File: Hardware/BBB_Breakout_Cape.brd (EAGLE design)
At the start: 86.4 x 54.6 mm, 20 parts, among them U1 EEPROM-I2CSMD

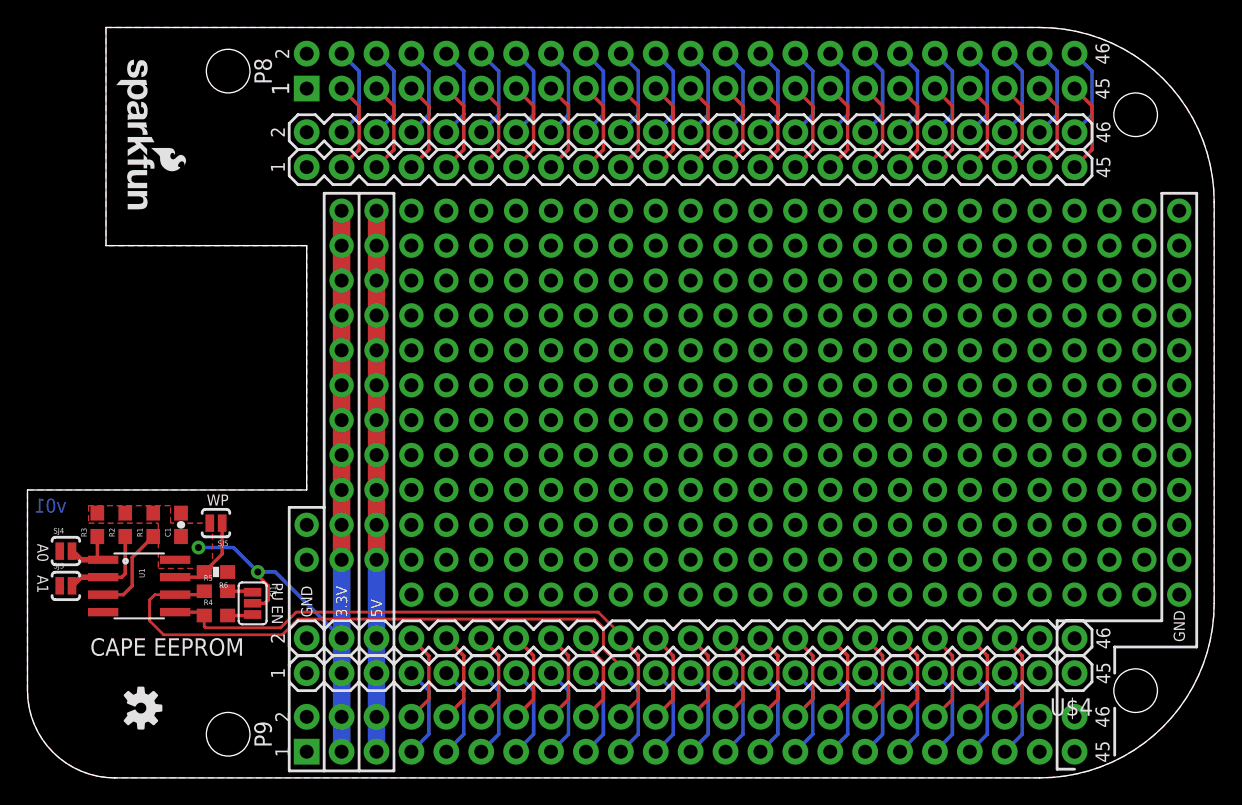
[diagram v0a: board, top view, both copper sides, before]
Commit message: added LEDS
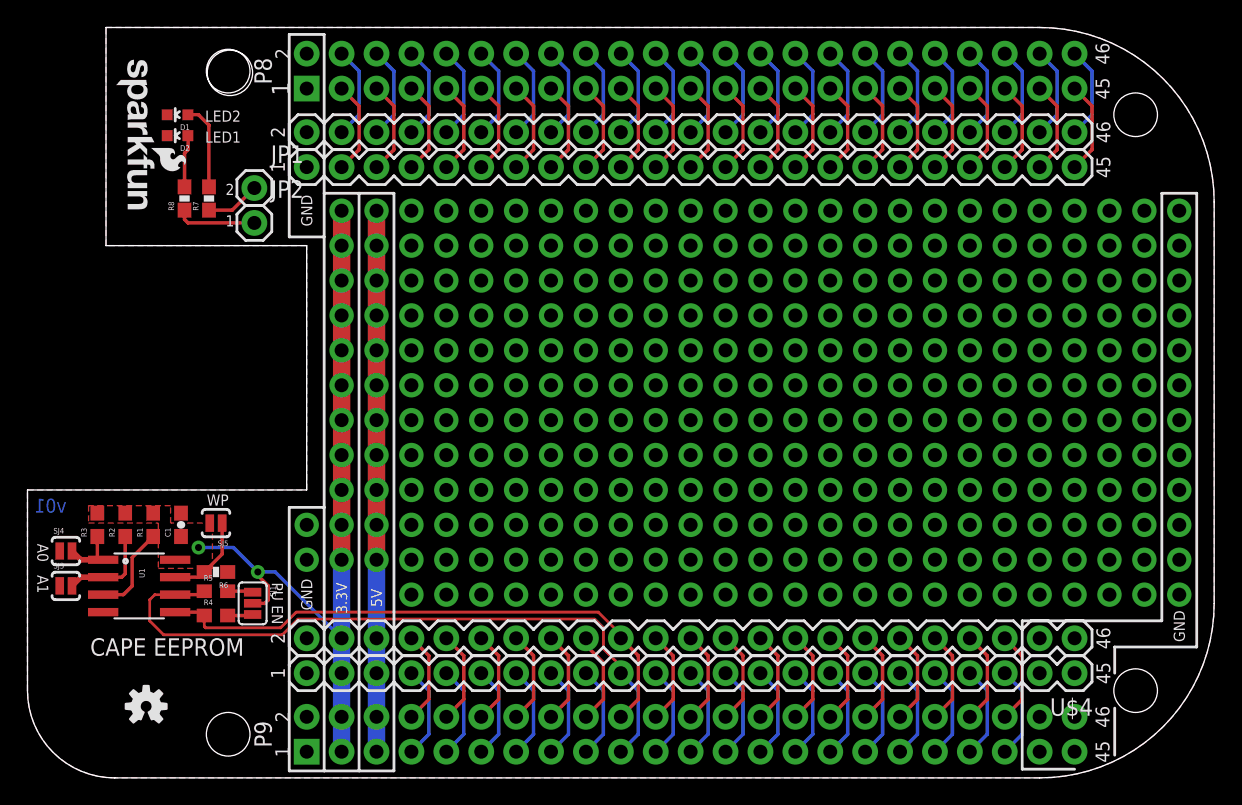
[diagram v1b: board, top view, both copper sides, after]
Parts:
- added D1, D2: RED, SparkFun-LED:LED-0603
- added JP1, JP2: M01PTH, SparkFun-Connectors:1X01
- added R7, R8: 1K, SparkFun-Resistors:0603-RES
- added STANDOFF1: STAND-OFF, SparkFun-Electromechanical:STAND-OFF
- moved LOGO2 0.40 mm to (8.64, 5.21), turned to 0 degrees
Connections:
- new net N$3: D1.A, R7.2
- new net N$30: JP2.1, R8.1
- new net N$7: D2.A, R8.2
- new net N$8: JP1.1, R7.1
- net GND: now also D1.C, D2.C
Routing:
- net N$3: track 0.00 -> 6.34 mm
- net N$30: track 0.00 -> 5.86 mm
- net N$8: track 0.00 -> 3.97 mm
- net N$7: track 0.00 -> 3.83 mm
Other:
- board text added: "LED1"
- board text added: "LED2"

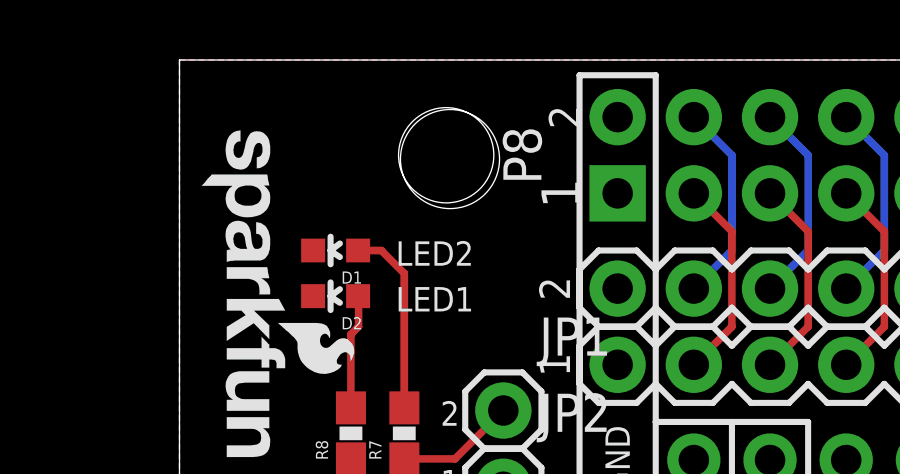
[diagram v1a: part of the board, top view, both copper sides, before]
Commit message: added more labels and fixed drill hole
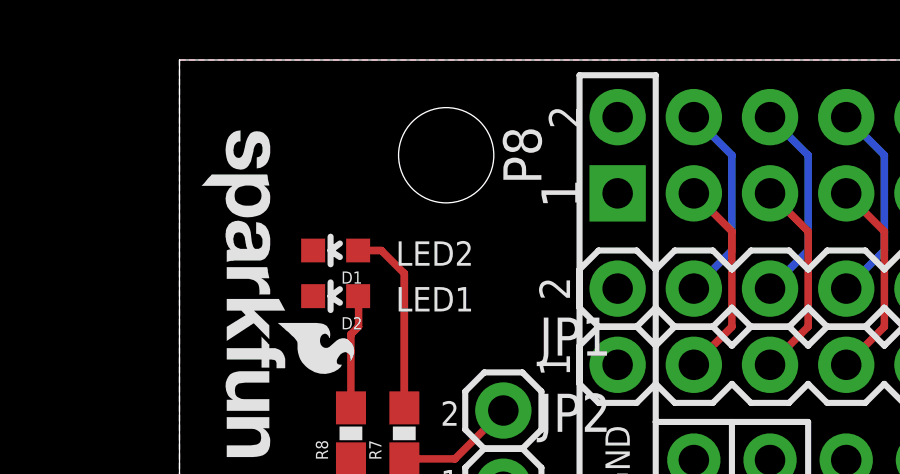
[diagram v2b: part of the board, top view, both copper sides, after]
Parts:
- removed STANDOFF1: STAND-OFF, SparkFun-Electromechanical:STAND-OFF
- added U$6: (no value), SparkFun-Aesthetics:SFE_LOGO_NAME_FLAME_.1
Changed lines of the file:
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@@
 <text x="14.732" y="40.132" size="0.8128" layer="21" font="vector" ratio="15" align="bottom-center">1</text>
 <text x="14.732" y="42.418" size="0.8128" layer="21" font="vector" ratio="15" align="bottom-center">2</text>
+<text x="14.732" y="42.418" size="0.8128" layer="22" font="vector" ratio="15" rot="MR0" align="bottom-center">2</text>
+<text x="14.732" y="40.132" size="0.8128" layer="22" font="vector" ratio="15" rot="MR0" align="bottom-center">1</text>
 </plain>
 <attributes>
@@
 <element name="JP1" library="SparkFun-Connectors" package="1X01" value="M01PTH" x="16.51" y="42.926"/>
 <element name="JP2" library="SparkFun-Connectors" package="1X01" value="M01PTH" x="16.51" y="40.386"/>
-<element name="STANDOFF1" library="SparkFun-Electromechanical" package="STAND-OFF" value="STAND-OFF" x="14.732" y="51.308"/>
+<element name="U$6" library="SparkFun-Aesthetics" package="SFE_LOGO_NAME_FLAME_.1" value="" x="7.874" y="4.318" rot="MR90"/>
 </elements>
 <signals>

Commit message: added version number
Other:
- board text added: "v10"
- board text removed: "v01"
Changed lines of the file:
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@@
 <wire x1="21.59" y1="6.858" x2="21.59" y2="0.508" width="0.2032" layer="21"/>
 <wire x1="24.13" y1="0.508" x2="24.13" y2="6.858" width="0.2032" layer="21"/>
-<text x="0.508" y="20.32" size="1.016" layer="16" font="vector" ratio="15" rot="MR180">v01</text>
+<text x="0.508" y="20.32" size="1.016" layer="16" font="vector" ratio="15" rot="MR180">v10</text>
 <text x="20.32" y="40.132" size="0.8128" layer="22" font="vector" ratio="15" rot="SMR270" align="center-right">GND</text>
 <text x="20.32" y="40.132" size="0.8128" layer="21" font="vector" ratio="15" rot="R270" align="center-right">GND</text>

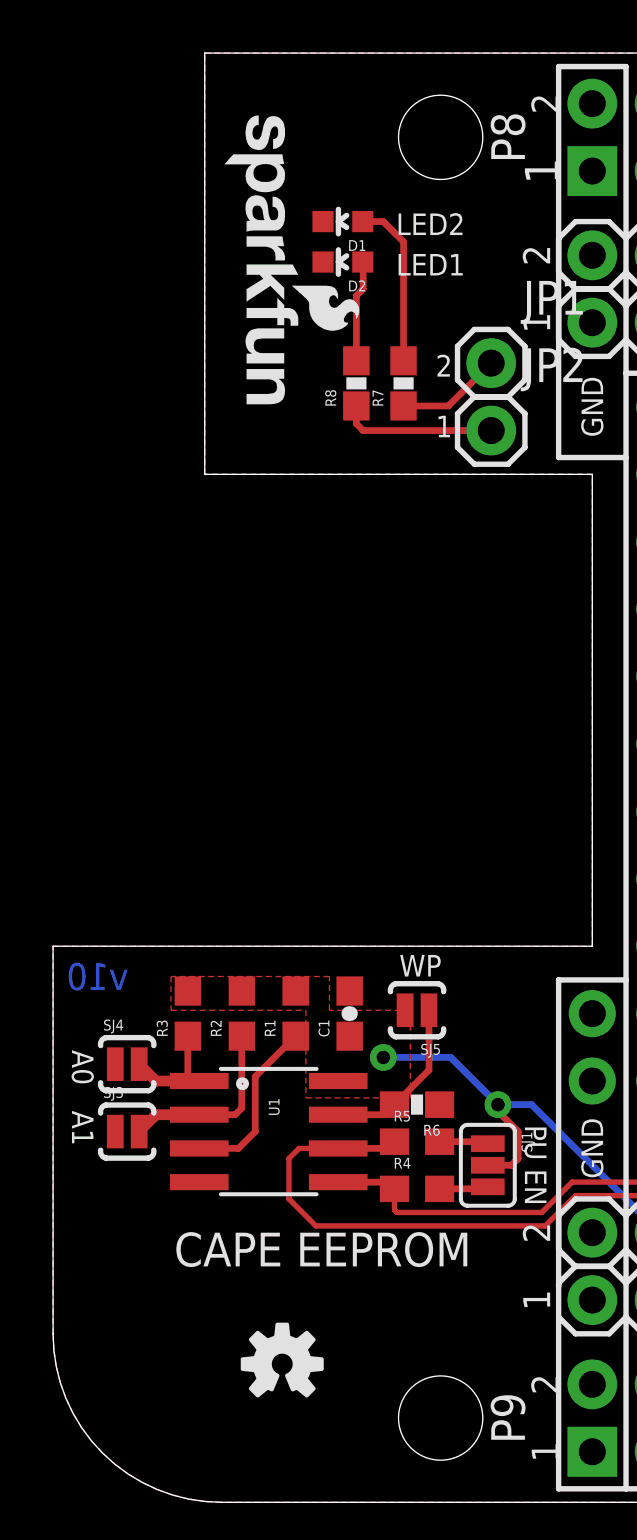
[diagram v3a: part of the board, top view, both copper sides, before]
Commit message: added local fiducials
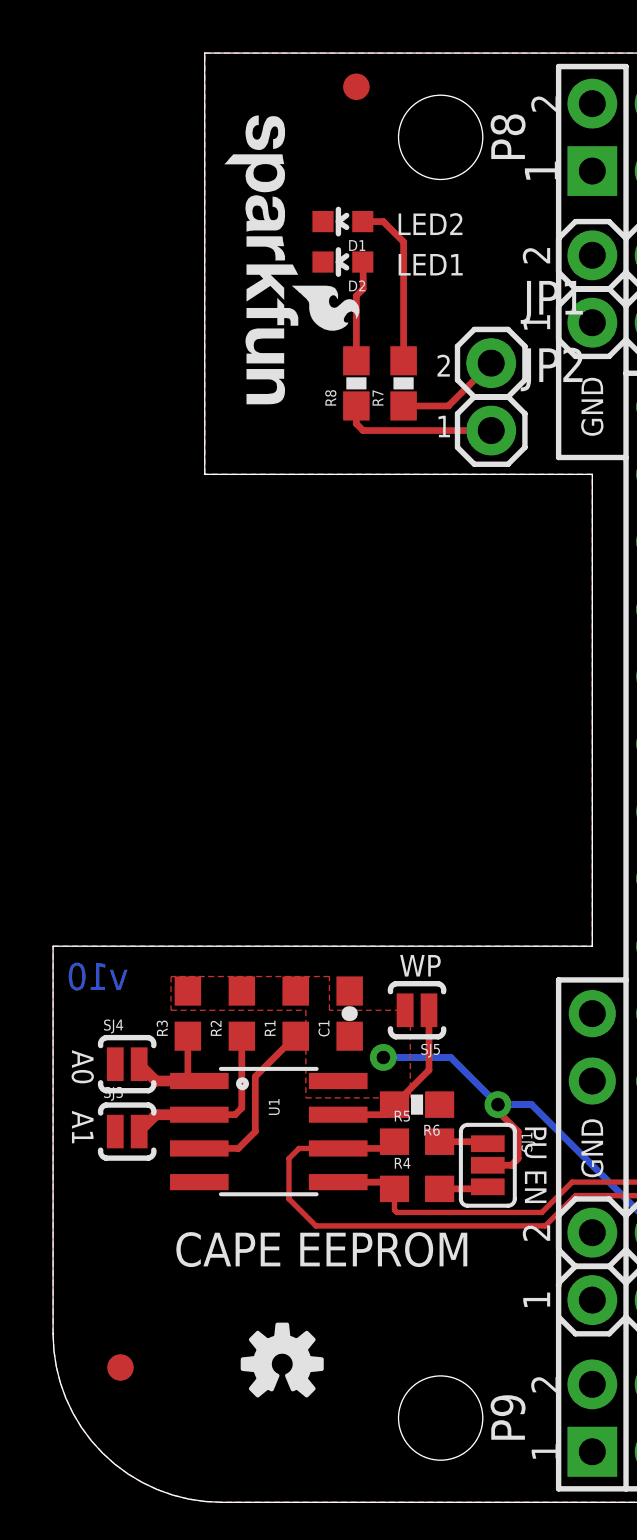
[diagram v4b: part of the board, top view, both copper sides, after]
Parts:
- added FID1, FID2: FIDUCIAL1X2, SparkFun-Aesthetics:FIDUCIAL-1X2
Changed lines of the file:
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@@
 <setting verticaltext="up"/>
 </settings>
-<grid distance="0.01" unitdist="inch" unit="inch" style="lines" multiple="1" display="yes" altdistance="0.005" altunitdist="inch" altunit="inch"/>
+<grid distance="0.05" unitdist="inch" unit="inch" style="lines" multiple="1" display="yes" altdistance="0.01" altunitdist="inch" altunit="inch"/>
 <layers>
 <layer number="1" name="Top" color="4" fill="1" visible="yes" active="yes"/>
@@
 <layer number="18" name="Vias" color="2" fill="1" visible="yes" active="yes"/>
 <layer number="19" name="Unrouted" color="6" fill="1" visible="yes" active="yes"/>
-<layer number="20" name="Dimension" color="15" fill="1" visible="yes" active="yes"/>
-<layer number="21" name="tPlace" color="16" fill="1" visible="yes" active="yes"/>
-<layer number="22" name="bPlace" color="14" fill="1" visible="yes" active="yes"/>
+<layer number="20" name="Dimension" color="6" fill="1" visible="yes" active="yes"/>
+<layer number="21" name="tPlace" color="6" fill="1" visible="yes" active="yes"/>
+<layer number="22" name="bPlace" color="6" fill="1" visible="yes" active="yes"/>
 <layer number="23" name="tOrigins" color="15" fill="1" visible="yes" active="yes"/>
 <layer number="24" name="bOrigins" color="15" fill="1" visible="yes" active="yes"/>
@@
 <element name="JP2" library="SparkFun-Connectors" package="1X01" value="M01PTH" x="16.51" y="40.386"/>
 <element name="U$6" library="SparkFun-Aesthetics" package="SFE_LOGO_NAME_FLAME_.1" value="" x="7.874" y="4.318" rot="MR90"/>
+<element name="FID1" library="SparkFun-Aesthetics" package="FIDUCIAL-1X2" value="FIDUCIAL1X2" x="2.54" y="5.08"/>
+<element name="FID2" library="SparkFun-Aesthetics" package="FIDUCIAL-1X2" value="FIDUCIAL1X2" x="11.43" y="53.34"/>
 </elements>
 <signals>

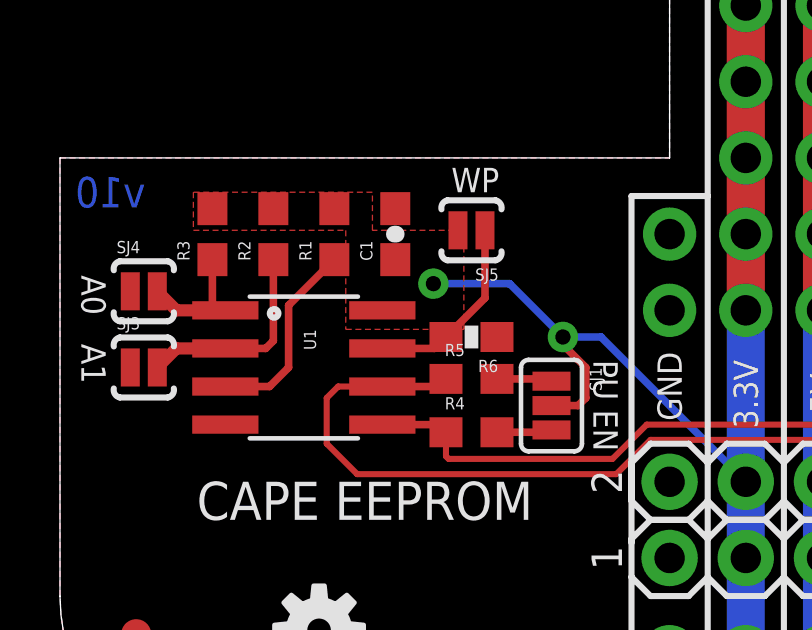
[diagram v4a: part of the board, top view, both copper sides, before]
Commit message: Updated juper packages on design and panel.  This only effects tcream layer.
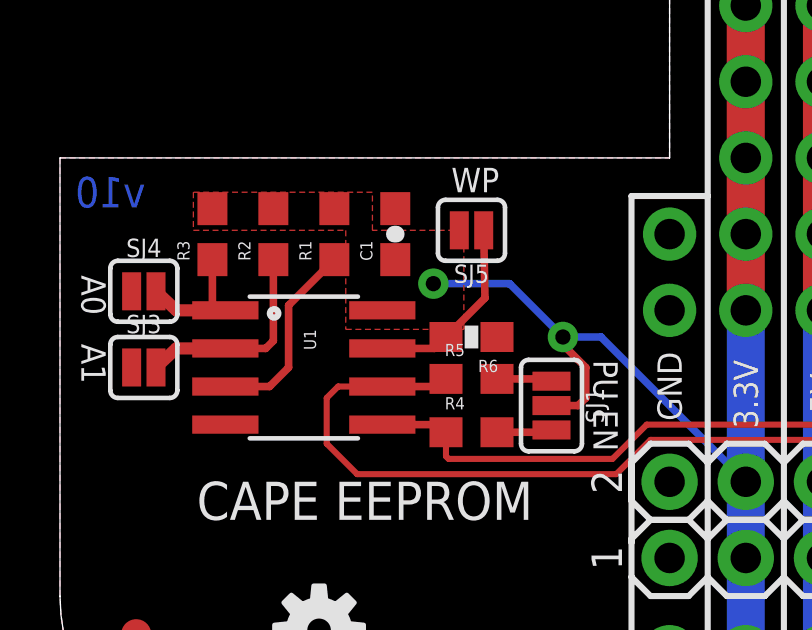
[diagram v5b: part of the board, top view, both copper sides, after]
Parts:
- R1, R2, R3, R4, R5: device SparkFun-Resistors:0603 -> SparkFun-Resistors:0603@1
- SJ1: device SparkFun-Passives:SJ_3_PASTE1&2&3 -> SparkFun-Jumpers:SMT-JUMPER_3_2-NC_PASTE_SILK
- SJ3, SJ4, SJ5: device SparkFun-Passives:SJ_2S-NO -> SparkFun-Jumpers:SMT-JUMPER_2_NO_SILK
